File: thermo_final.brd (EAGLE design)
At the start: 67.8 x 89 mm, 109 parts

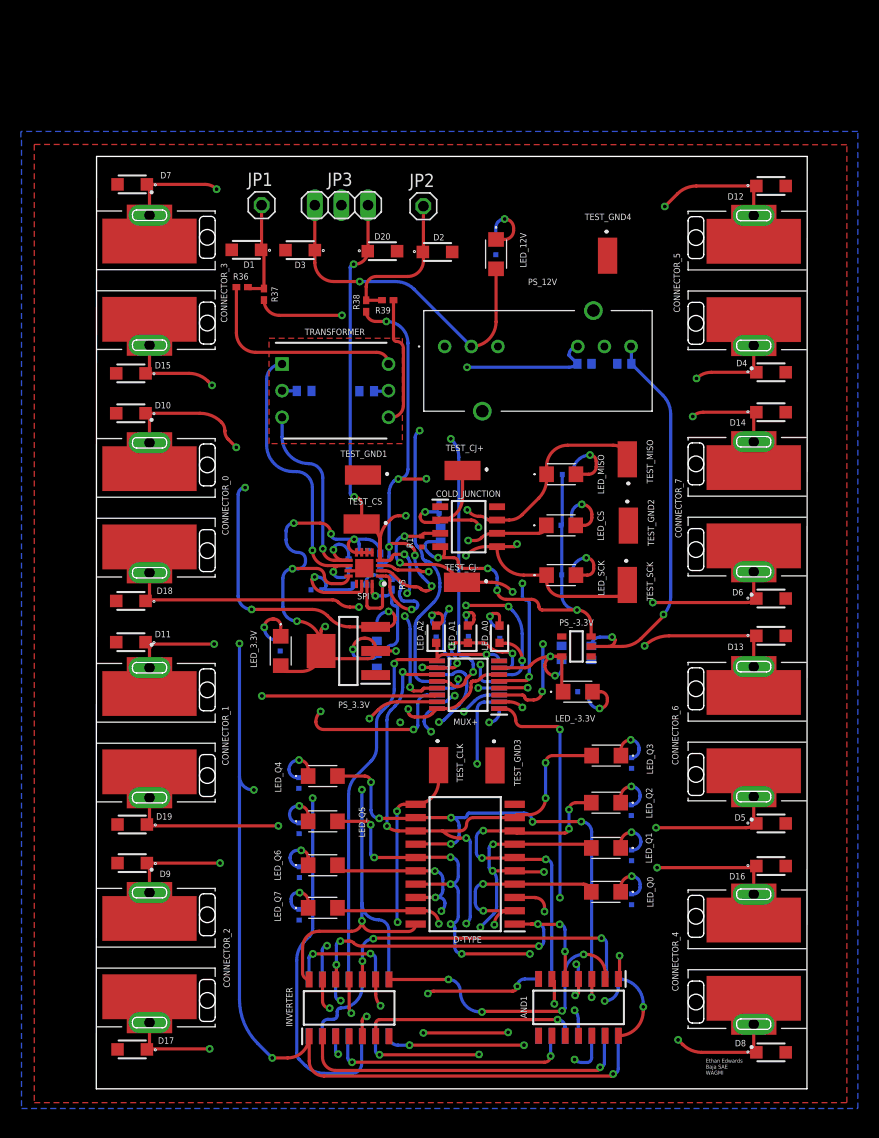
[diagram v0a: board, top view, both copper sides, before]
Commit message: Final w/GND vias & Enclosure Holes
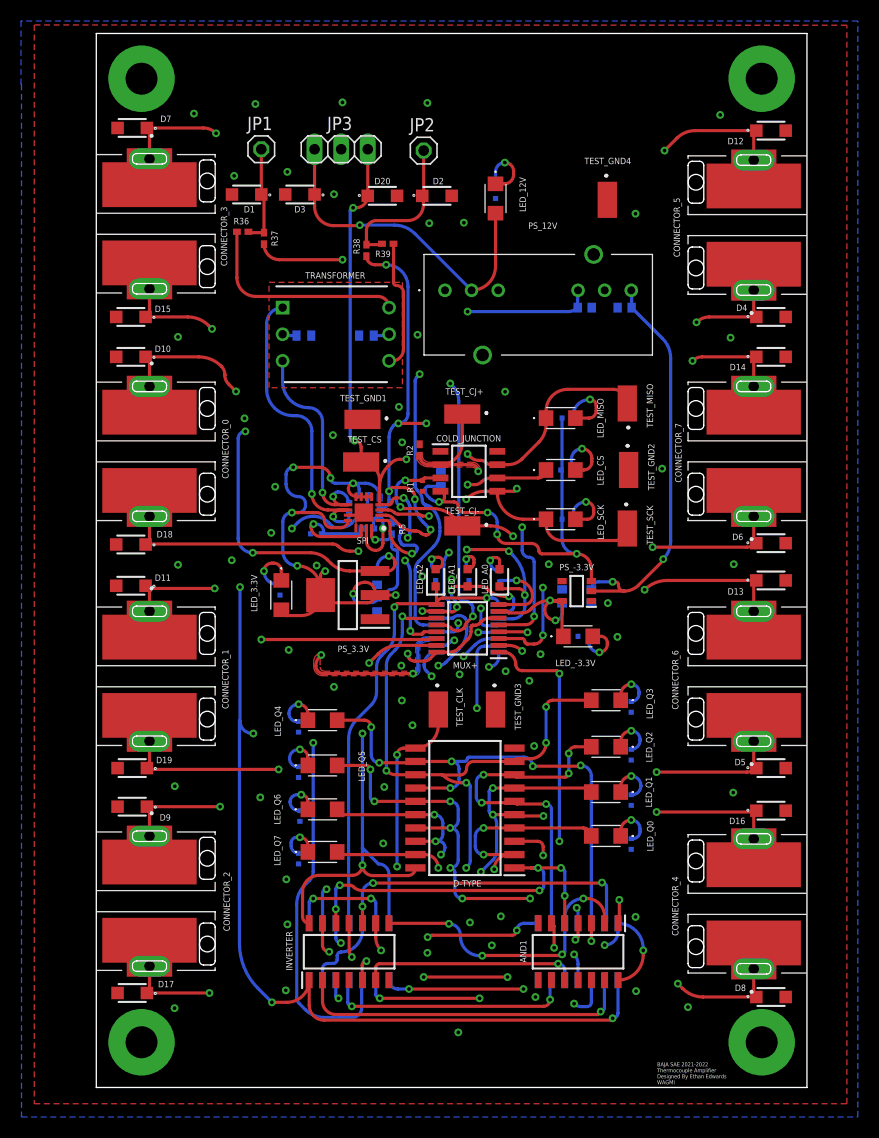
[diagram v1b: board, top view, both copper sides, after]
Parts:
- added U$1, U$2, U$3, U$4: THROUGH_HOLE, SamacSys_Parts:THROUGH_HOLE
- R2: value 5.6K -> CRG0402ZR; device SamacSys_Parts:ERA2AED122X -> SamacSys_Parts:RESC1005X40N
- moved TEST_CS 5.92 mm to (25.3, 59.7)
- moved R2 5.84 mm to (30.9, 60.8), flipped to the top, turned to 90 degrees
- moved R14 5.41 mm to (25.9, 53.3)
- moved R30 5.39 mm to (32.4, 48.9)
- moved C2 5.39 mm to (44.5, 46.9)
- moved LED_A2 5.39 mm to (32.4, 48.6)
- moved MUX+ 5.39 mm to (35.4, 43.8)
- moved MUX- 5.39 mm to (35.4, 43.8)
- moved R3 5.39 mm to (24.1, 55.4)
- moved TRANSFORMER 5.39 mm to (22.9, 71.9)
- moved C7 5.38 mm to (26.8, 46.1)
- moved LED_A1 5.38 mm to (35.4, 48.6)
- moved R28 5.38 mm to (38.5, 48.8)
- moved R8 5.38 mm to (45.0, 63.9)
- moved TEST_CJ+ 5.38 mm to (34.9, 64.3)
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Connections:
- net CJ-: now also R2.1; no longer C1.1, R2.2
- net GND: now also C1.1, R2.2; no longer R2.1
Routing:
- net GND: track 1.97 -> 20.6 mm, vias 0 -> 59
- net CJ-: track 54.4 -> 51.0 mm, vias 4 -> 3
- net V+: track 68.2 -> 67.3 mm
- net N$11: track 8.32 -> 7.56 mm
- net -VCC: track 33.2 -> 33.9 mm
- net IM: track 21.5 -> 20.9 mm
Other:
- board size 67.8 x 89 mm -> 67.8 x 100.6 mm
- board text added: "BAJA SAE 2021-2022 Thermocouple Amplifier Designed By Ethan Edwards WAGMI"
- board text removed: "Ethan Edwards Baja SAE WAGMI"

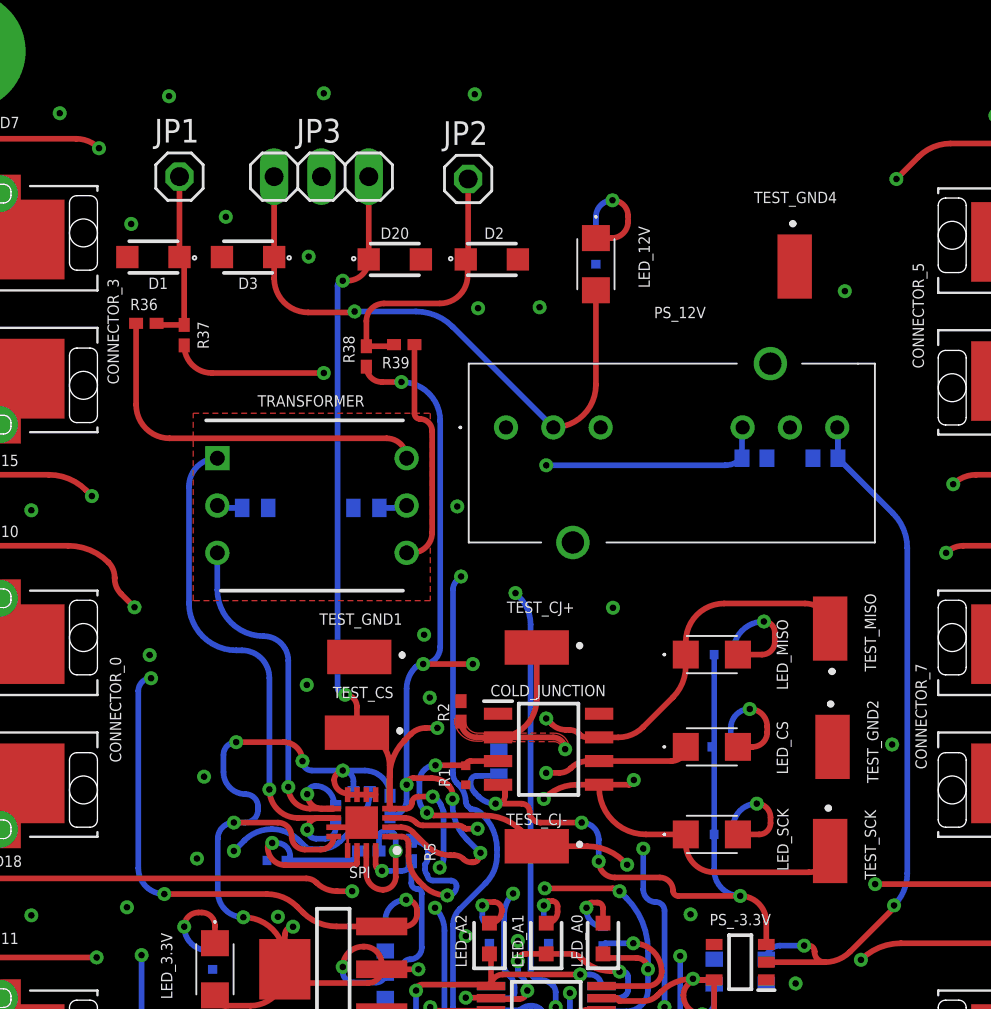
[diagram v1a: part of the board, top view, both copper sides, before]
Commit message: Rearranged transformer
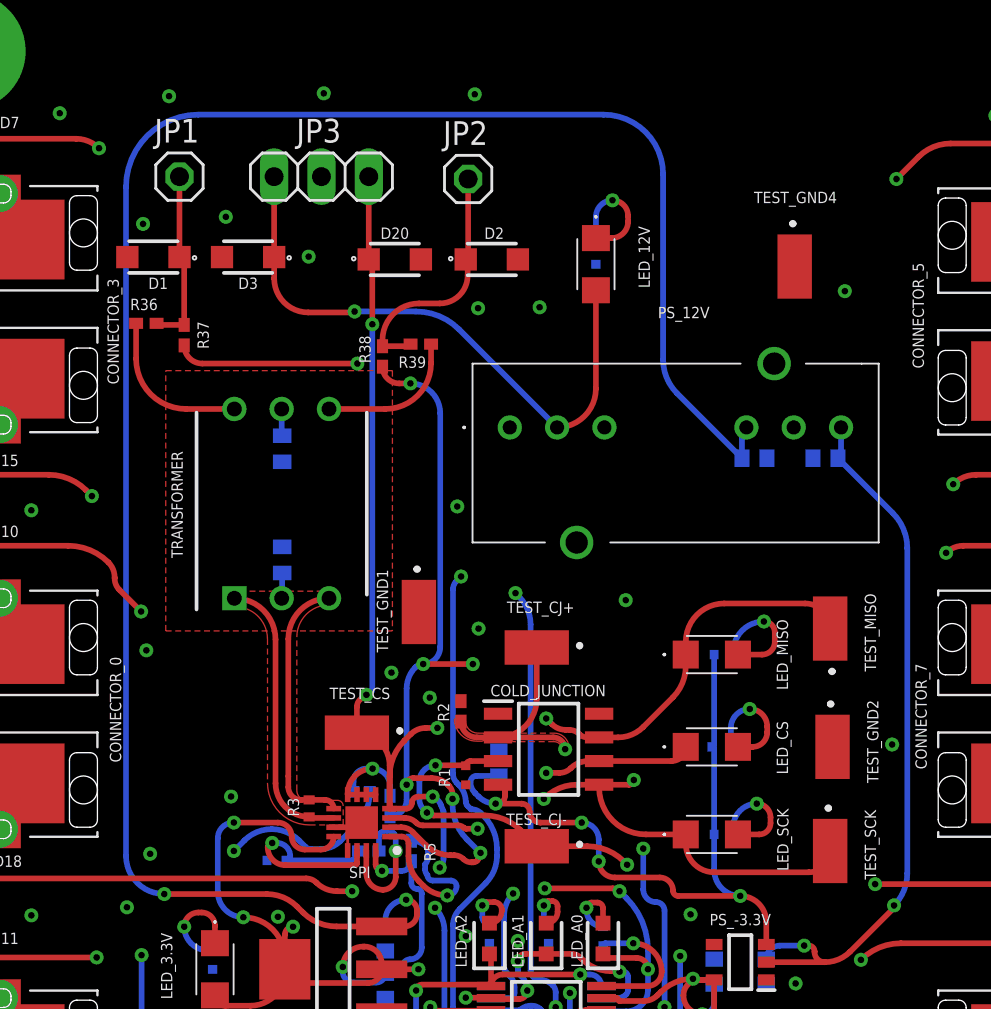
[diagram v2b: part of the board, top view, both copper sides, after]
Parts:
- moved C10 5.52 mm to (21.3, 74.9), turned to 270 degrees
- moved TEST_GND1 4.01 mm to (28.6, 66.2), turned to 90 degrees
- moved C9 3.15 mm to (21.3, 69.0), turned to 270 degrees
- moved TRANSFORMER 1.63 mm to (21.2, 72.0), turned to 90 degrees
- moved R3 1.44 mm to (22.7, 55.6), flipped to the top
- moved R39 0.89 mm to (28.7, 80.5)
- moved R38 0.86 mm to (26.6, 79.9)
- moved PS_12V 0.20 mm to (33.5, 76.1)
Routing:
- net V+: track 67.3 -> 106.2 mm, vias 4 -> 2
- net IP: track 28.5 -> 14.8 mm, vias 2 -> 0
- net IPOUT: track 20.1 -> 8.29 mm
- net IM: track 20.9 -> 14.0 mm, vias 2 -> 0
- net IMOUT: track 12.3 -> 7.52 mm
- net T3-: track 49.7 -> 54.4 mm
- net VCC: track 248.4 -> 245.6 mm, vias 21 -> 19
- net N$40: track 14.7 -> 13.2 mm
- net CS: track 199.9 -> 199.1 mm
- net MISO: track 67.6 -> 67.0 mm
- net SCK: track 66.7 -> 67.3 mm
